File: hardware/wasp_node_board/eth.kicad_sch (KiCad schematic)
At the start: 25 parts, among them J2 RJ45_Hanrun_HR911105A_Horizon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, J4 RJ45_Hanrun_HR911105A_Horizon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, J5 RJ45_Hanrun_HR911105A_Horizon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, U5 KSZ8794CNXCC, Y1 TSX-3225 25.00M-N0YYYYG30RGB

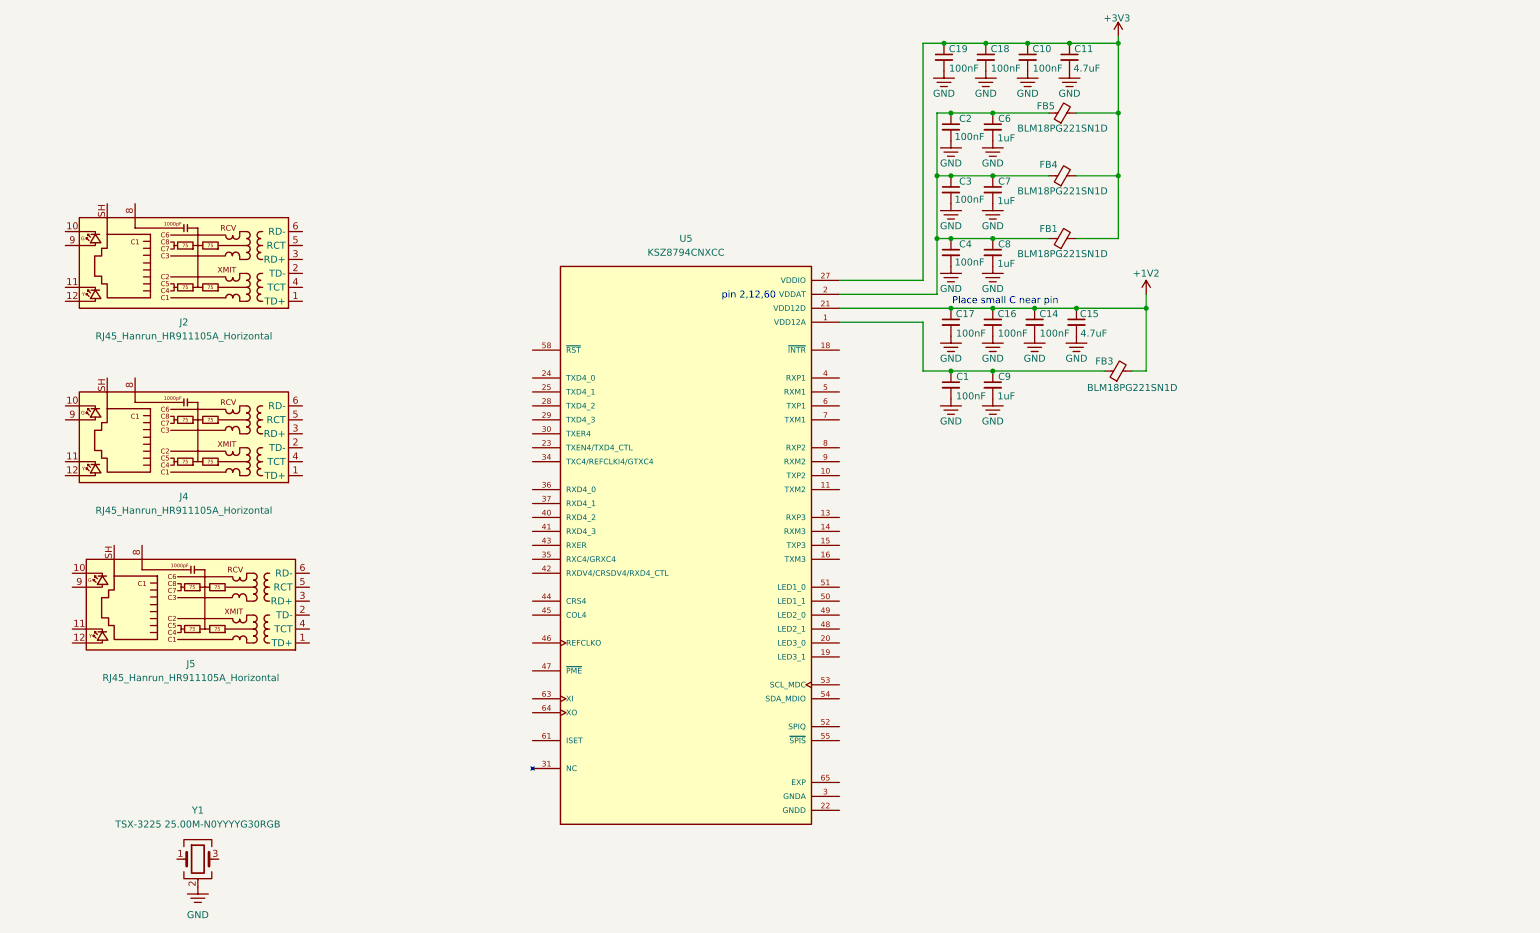
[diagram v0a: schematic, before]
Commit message: Node board schematic complete — MCU, switch, PSRAM, power and expansion
Co-Authored-By: Claude Opus 5 <noreply@anthropic.com>
Claude-Session: https://claude.ai/code/session_01R5uaLk4w44r9dBy8LCo6if
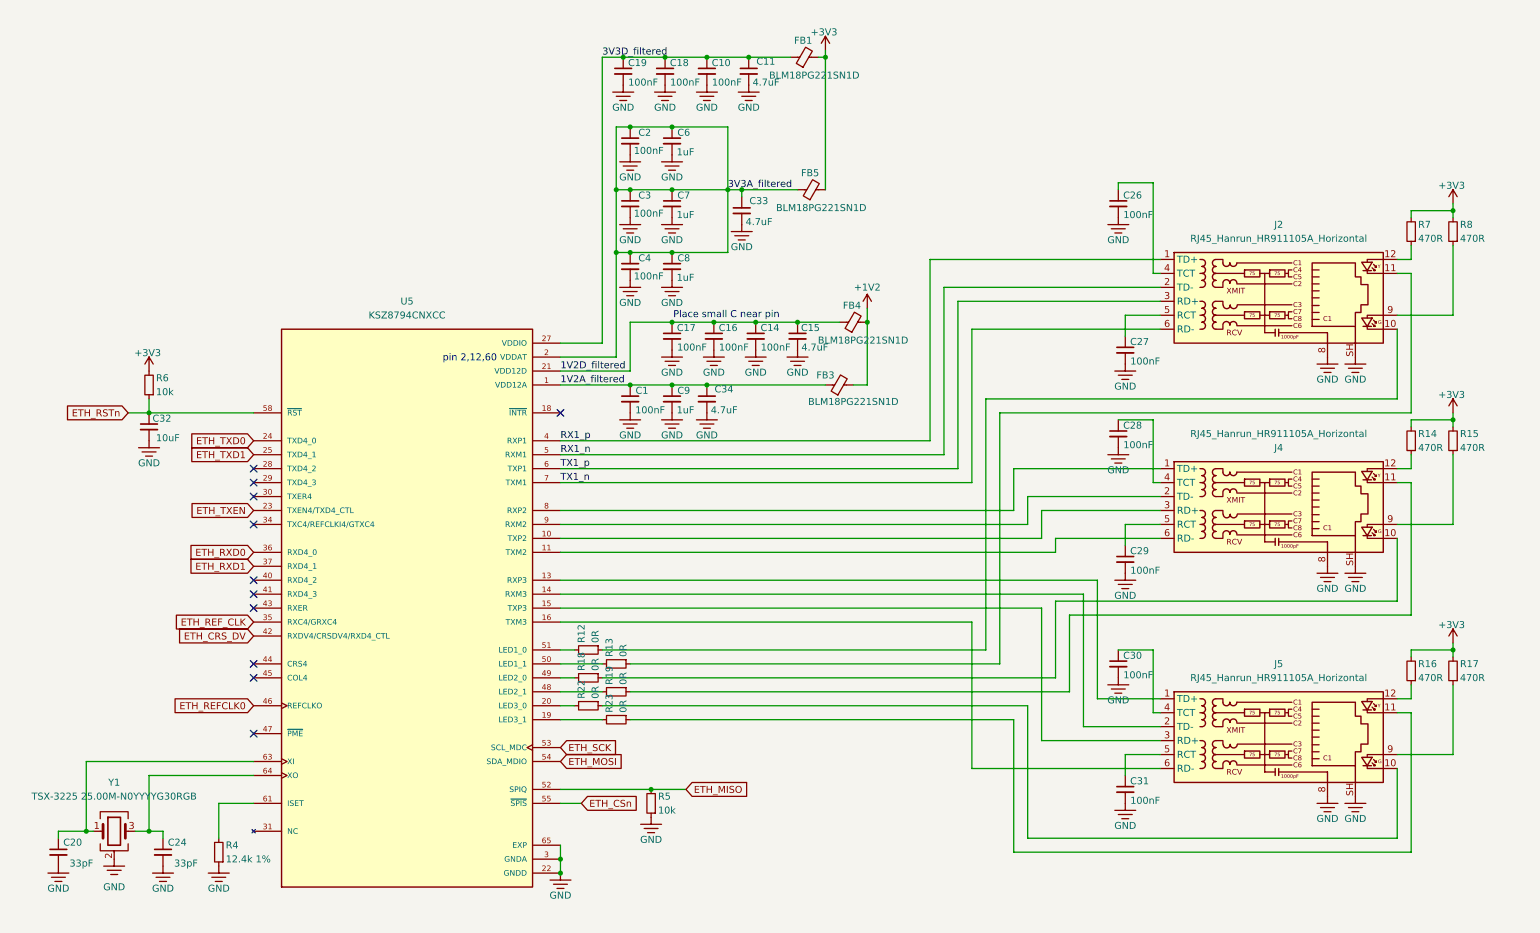
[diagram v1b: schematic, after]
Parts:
- added C20, C24: 33pF, Capacitor_SMD:C_0402_1005Metric, symbol Device:C_Small
- added C26, C27, C28, C29, C30, C31: 100nF, Capacitor_SMD:C_0402_1005Metric, symbol Device:C_Small
- added C32: 10uF, Capacitor_SMD:C_0603_1608Metric, symbol Device:C_Small
- added C33, C34: 4.7uF, Capacitor_SMD:C_0603_1608Metric, symbol Device:C_Small
- added R12, R13, R18, R19, R22, R23: 0R, Resistor_SMD:R_0402_1005Metric, symbol Device:R_Small
- added R14, R15, R16, R17, R7, R8: 470R, Resistor_SMD:R_0402_1005Metric, symbol Device:R_Small
- added R4: 12.4k 1%, Resistor_SMD:R_0402_1005Metric, symbol Device:R_Small
- added R5, R6: 10k, Resistor_SMD:R_0402_1005Metric, symbol Device:R_Small
- U5: footprint KSZ8794CNXCC:IC_KSZ8794CNXCC -> Package_DFN_QFN:QFN-64-1EP_8x8mm_P0.4mm_EP6.5x6.5mm_ThermalVias
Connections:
- net GNDA is gone; now on net GND: U5.17 (GNDA), U5.3 (GNDA), U5.62 (GNDA)
- net GNDD is gone; now on net GND: U5.22 (GNDD), U5.26 (GNDD), U5.32 (GNDD), U5.38 (GNDD), U5.57 (GNDD)
- net +1V2: now also FB4.2; no longer C14.1, C15.1, C16.1, C17.1, U5.21 (VDD12D), U5.33 (VDD12D), U5.59 (VDD12D)
- net +3V3: now also R14.2, R15.2, R16.2, R17.2, R6.2, R7.2, R8.2; no longer C10.1, C11.1, C18.1, C19.1, FB4.2, U5.27 (VDDIO), U5.39 (VDDIO), U5.56 (VDDIO)
- net GND: now also J2.8, J2.SH, J4.8, J4.SH, J5.8, J5.SH, U5.65 (EXP), C20.2, C24.2, C26.2, C27.2, C28.2, C29.2, C30.2, C31.2, C32.2, C33.2, C34.2, R4.1, R5.1
- net VDDAT: now also C33.1; no longer FB1.1, FB4.1
- net 1V2A_filtered: now reaches C1.1, C9.1, FB3.1, U5.1 (VDD12A)
- net 1V2A_filtered: now also C34.1
- net at J5.1 (TD+): now also U5.13 (RXP3)
- net at J5.10: now also R22.1
- net at J5.11: now also R23.1
- net at J5.12: now also R16.1
- net at J5.2 (TD-): now also U5.14 (RXM3)
- net at J5.3 (RD+): now also U5.15 (TXP3)
- net at J5.4 (TCT): now also C30.1
- net at J5.5 (RCT): now also C31.1
- net at J5.6 (RD-): now also U5.16 (TXM3)
- net at J5.9: now also R17.1
- net at U5.10 (TXP2): now also J4.3 (RD+)
- net at U5.11 (TXM2): now also J4.6 (RD-)
- net at U5.19 (LED3_1): now also R23.2
- net at U5.20 (LED3_0): now also R22.2
- net ETH_TXEN: now reaches U5.23 (TXEN4/TXD4_CTL)
- net ETH_TXD0: now reaches U5.24 (TXD4_0)
- net ETH_TXD1: now reaches U5.25 (TXD4_1)
- net ETH_REF_CLK: now reaches U5.35 (RXC4/GRXC4)
- net ETH_RXD0: now reaches U5.36 (RXD4_0)
- net ETH_RXD1: now reaches U5.37 (RXD4_1)
- net RX1_p: now reaches U5.4 (RXP1)
- net RX1_p: now also J2.1 (TD+)
- net ETH_CRS_DV: now reaches U5.42 (RXDV4/CRSDV4/RXD4_CTL)
- net ETH_REFCLK0: now reaches U5.46 (REFCLKO)
- net at U5.48 (LED2_1): now also R19.2
- net at U5.49 (LED2_0): now also R18.2
- net RX1_n: now reaches U5.5 (RXM1)
- net RX1_n: now also J2.2 (TD-)
- net at U5.50 (LED1_1): now also R13.2
- net at U5.51 (LED1_0): now also R12.2
- net ETH_MISO: now reaches U5.52 (SPIQ)
- net ETH_MISO: now also R5.2
- net ETH_SCK: now reaches U5.53 (SCL_MDC)
- net ETH_MOSI: now reaches U5.54 (SDA_MDIO)
- net ETH_CSn: now reaches U5.55 (~{SPIS})
- net ETH_RSTn: now reaches U5.58 (~{RST})
- net ETH_RSTn: now also C32.1, R6.1
- net TX1_p: now reaches U5.6 (TXP1)
- net TX1_p: now also J2.3 (RD+)
- net at U5.61 (ISET): now also R4.2
- net at U5.63 (XI): now also Y1.1, C20.1
- net at U5.64 (XO): now also Y1.3, C24.1
- net TX1_n: now reaches U5.7 (TXM1)
- net TX1_n: now also J2.6 (RD-)
- net at U5.8 (RXP2): now also J4.1 (TD+)
- net at U5.9 (RXM2): now also J4.2 (TD-)
- net at J2.10: now also R12.1
- net at J2.11: now also R13.1
- net at J2.12: now also R7.1
- net at J2.4 (TCT): now also C26.1
- net at J2.5 (RCT): now also C27.1
- net at J2.9: now also R8.1
- net at J4.10: now also R18.1
- net at J4.11: now also R19.1
- net at J4.12: now also R14.1
- net at J4.4 (TCT): now also C28.1
- net at J4.5 (RCT): now also C29.1
- net at J4.9: now also R15.1
- new net VDD12D: C14.1, C15.1, C16.1, C17.1, FB4.1, U5.21 (VDD12D), U5.33 (VDD12D), U5.59 (VDD12D)
- new net VDDIO: C10.1, C11.1, C18.1, C19.1, FB1.1, U5.27 (VDDIO), U5.39 (VDDIO), U5.56 (VDDIO)
- no-connect marks 0 -> 11
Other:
- moved on the sheet: C1, C10, C11, C14, C15, C16, C17, C18, C19, C2, C3, C4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

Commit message: Schematic verified clean and layout started
Co-Authored-By: Claude Opus 5 <noreply@anthropic.com>
Claude-Session: https://claude.ai/code/session_01R5uaLk4w44r9dBy8LCo6if
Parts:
- U5: footprint Package_DFN_QFN:QFN-64-1EP_8x8mm_P0.4mm_EP6.5x6.5mm_ThermalVias -> KSZ8794CNXCC:IC_KSZ8794CNXCC
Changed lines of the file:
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@@
 			)
 		)
-		(property "Description" ""
+		(property "Description" "Resistor, small symbol"
 			(at 267.97 52.07 0)
 			(effects
@@
 			)
 		)
-		(property "Description" ""
+		(property "Description" "Resistor, small symbol"
 			(at 123.19 135.89 0)
 			(effects
@@
 			)
 		)
-		(property "Description" ""
+		(property "Description" "Resistor, small symbol"
 			(at 50.8 165.1 0)
 			(effects
@@
 			)
 		)
-		(property "Description" ""
+		(property "Description" "Resistor, small symbol"
 			(at 118.11 128.27 0)
 			(effects
@@
 			)
 		)
-		(property "Footprint" "Package_DFN_QFN:QFN-64-1EP_8x8mm_P0.4mm_EP6.5x6.5mm_ThermalVias"
+		(property "Footprint" "KSZ8794CNXCC:IC_KSZ8794CNXCC"
 			(at 85.09 120.65 0)
 			(effects
@@
 			)
 		)
-		(property "Description" ""
+		(property "Description" "Resistor, small symbol"
 			(at 129.54 156.21 0)
 			(effects
@@
 			)
 		)
-		(property "Description" ""
+		(property "Description" "Resistor, small symbol"
 			(at 38.1 80.01 0)
 			(effects
@@
 			)
 		)
-		(property "Description" ""
+		(property "Description" "Resistor, small symbol"
 			(at 118.11 133.35 0)
 			(effects
@@
 			)
 		)
-		(property "Description" ""
+		(property "Description" "Resistor, small symbol"
 			(at 275.59 132.08 0)
 			(effects
@@
 			)
 		)
-		(property "Description" ""
+		(property "Description" "Resistor, small symbol"
 			(at 123.19 130.81 0)
 			(effects
@@
 			)
 		)
-		(property "Description" ""
+		(property "Description" "Resistor, small symbol"
 			(at 118.11 138.43 0)
 			(effects
@@
 			)
 		)
-		(property "Description" ""
+		(property "Description" "Resistor, small symbol"
 			(at 267.97 132.08 0)
 			(effects
@@
 			)
 		)
-		(property "Description" ""
+		(property "Description" "Resistor, small symbol"
 			(at 267.97 90.17 0)
 			(effects
@@
 			)
 		)
-		(property "Description" ""
+		(property "Description" "Resistor, small symbol"
 			(at 275.59 52.07 0)
 			(effects
@@
 			)
 		)
-		(property "Description" ""
+		(property "Description" "Resistor, small symbol"
 			(at 123.19 140.97 0)
 			(effects
@@
 			)
 		)
-		(property "Description" ""
+		(property "Description" "Resistor, small symbol"
 			(at 275.59 90.17 0)
 			(effects

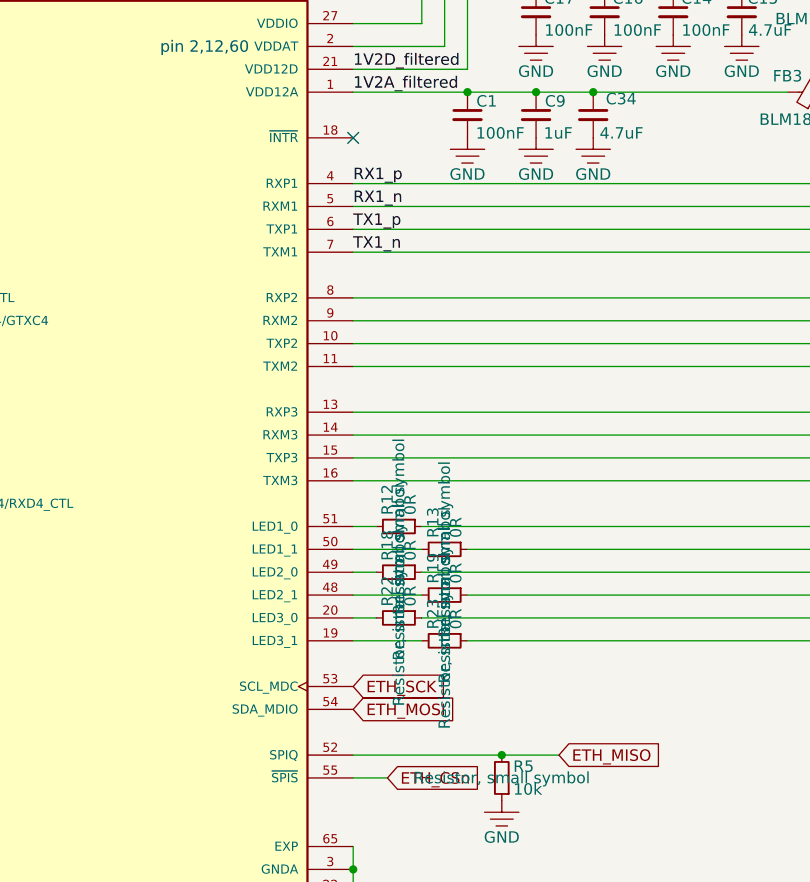
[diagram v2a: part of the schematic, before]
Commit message: Board setup for OSH Park — FR408 stackup, impedance net classes, DRC rules
Co-Authored-By: Claude Opus 5 <noreply@anthropic.com>
Claude-Session: https://claude.ai/code/session_01R5uaLk4w44r9dBy8LCo6if
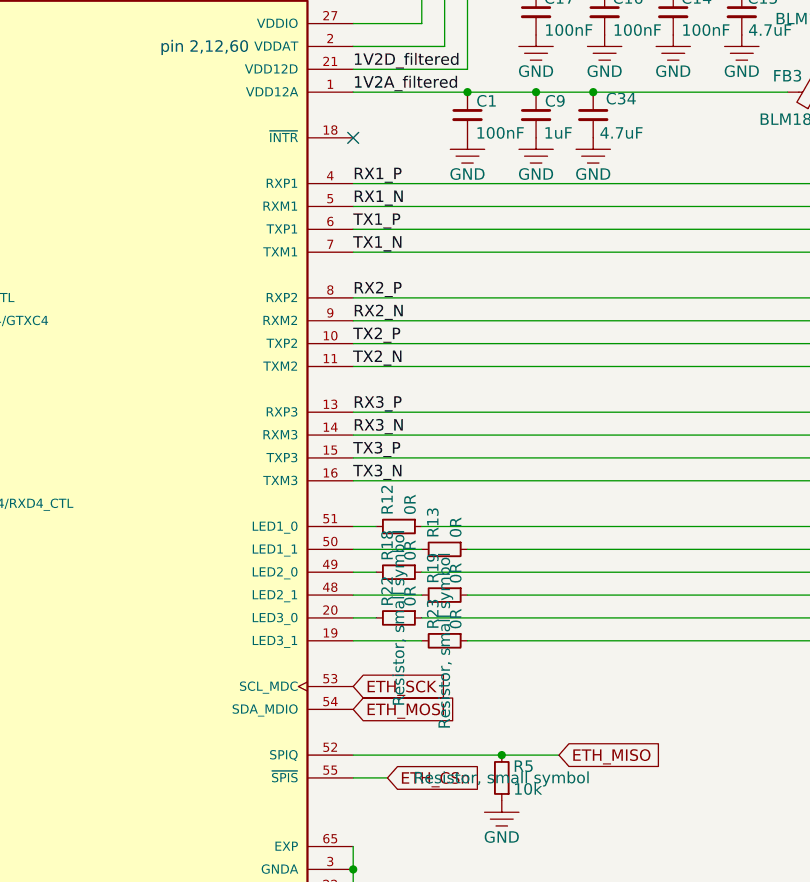
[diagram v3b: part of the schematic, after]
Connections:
- net RX3_P: now reaches J5.1 (TD+), U5.13 (RXP3)
- net RX3_N: now reaches J5.2 (TD-), U5.14 (RXM3)
- net TX3_P: now reaches J5.3 (RD+), U5.15 (TXP3)
- net TX3_N: now reaches J5.6 (RD-), U5.16 (TXM3)
- net TX2_P: now reaches J4.3 (RD+), U5.10 (TXP2)
- net TX2_N: now reaches J4.6 (RD-), U5.11 (TXM2)
- net RX2_P: now reaches J4.1 (TD+), U5.8 (RXP2)
- net RX2_N: now reaches J4.2 (TD-), U5.9 (RXM2)
- net RX1_n renamed RX1_N
- net RX1_p renamed RX1_P
- net TX1_n renamed TX1_N
- net TX1_p renamed TX1_P
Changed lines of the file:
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@@
 		)
 	)
-	(label "TX1_p"
+	(label "RX2_P"
+		(at 113.03 102.87 0)
+		(effects
+			(font
+				(size 1.27 1.27)
+			)
+			(justify left bottom)
+		)
+	)
+	(label "RX3_P"
+		(at 113.03 115.57 0)
+		(effects
+			(font
+				(size 1.27 1.27)
+			)
+			(justify left bottom)
+		)
+	)
+	(label "TX1_P"
 		(at 113.03 95.25 0)
 		(effects
@@
 		)
 	)
+	(label "TX3_P"
+		(at 113.03 120.65 0)
+		(effects
+			(font
+				(size 1.27 1.27)
+			)
+			(justify left bottom)
+		)
+	)
 	(label "1V2D_filtered"
 		(at 113.03 77.47 0)
@@
 		)
 	)
-	(label "TX1_n"
+	(label "TX1_N"
 		(at 113.03 97.79 0)
 		(effects
@@
 		)
 	)
+	(label "TX2_P"
+		(at 113.03 107.95 0)
+		(effects
+			(font
+				(size 1.27 1.27)
+			)
+			(justify left bottom)
+		)
+	)
+	(label "RX2_N"
+		(at 113.03 105.41 0)
+		(effects
+			(font
+				(size 1.27 1.27)
+			)
+			(justify left bottom)
+		)
+	)
 	(label "3V3D_filtered"
 		(at 120.65 20.32 0)
@@
 		)
 	)
-	(label "RX1_p"
+	(label "RX1_P"
 		(at 113.03 90.17 0)
 		(effects
@@
 		)
 	)
+	(label "TX3_N"
+		(at 113.03 123.19 0)
+		(effects
+			(font
+				(size 1.27 1.27)
+			)
+			(justify left bottom)
+		)
+	)
+	(label "RX3_N"
+		(at 113.03 118.11 0)
+		(effects
+			(font
+				(size 1.27 1.27)
+			)
+			(justify left bottom)
+		)
+	)
+	(label "TX2_N"
+		(at 113.03 110.49 0)
+		(effects
+			(font
+				(size 1.27 1.27)
+			)
+			(justify left bottom)
+		)
+	)
 	(label "1V2A_filtered"
 		(at 113.03 80.01 0)
@@
 		)
 	)
-	(label "RX1_n"
+	(label "RX1_N"
 		(at 113.03 92.71 0)
 		(effects
@@
 					(size 1.27 1.27)
 				)
+				(hide yes)
 			)
 		)
@@
 					(size 1.27 1.27)
 				)
+				(hide yes)
 			)
 		)
@@
 					(size 1.27 1.27)
 				)
+				(hide yes)
 			)
 		)
@@
 					(size 1.27 1.27)
 				)
+				(hide yes)
 			)
 		)
